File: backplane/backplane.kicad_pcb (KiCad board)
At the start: 2 copper layers, 142.8 x 197.5 mm, 20 parts, among them J1 Conn_01x10, J10 Conn_01x10, J11 Conn_01x10, J2 Conn_01x10, J4 48V in, J5 Conn_01x10, J6 Conn_01x10, J7 Conn_01x10, J8 Conn_01x10, J9 Conn_01x10

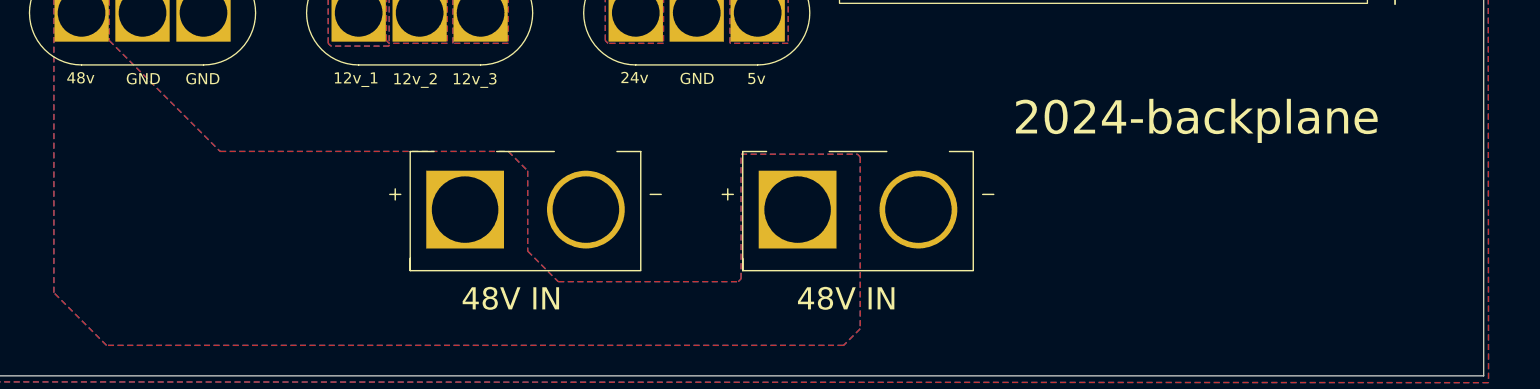
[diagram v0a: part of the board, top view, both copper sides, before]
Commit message: changed font thickness and added contributor
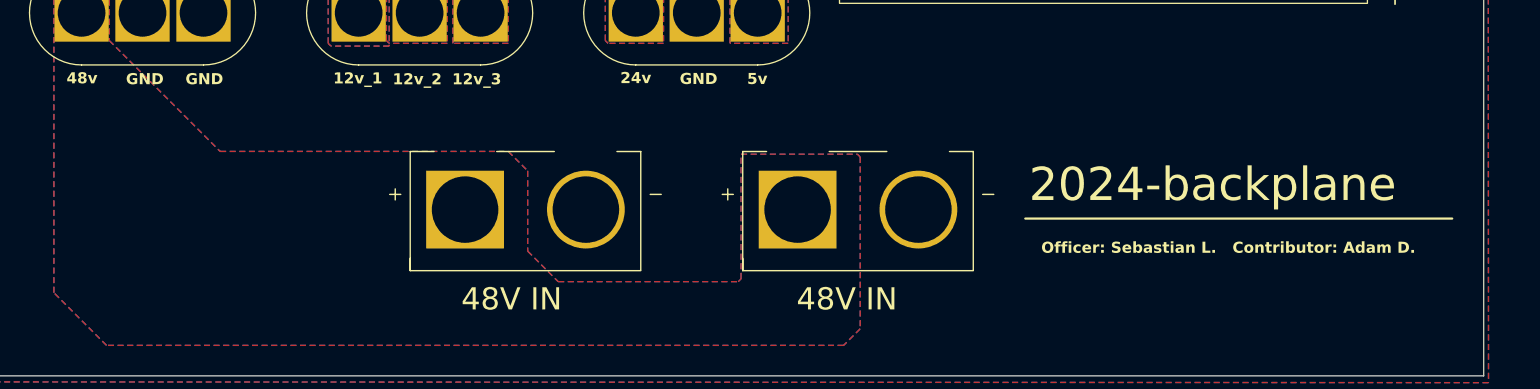
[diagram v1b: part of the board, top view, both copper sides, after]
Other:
- board text added: "Officer: Sebastian L. Contributor: Adam D."
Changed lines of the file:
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@@
   (gr_line (start 241 162.82) (end 241 219.22)
     (stroke (width 0.15) (type default)) (layer "F.SilkS"))
+  (gr_line (start 207.64 238.56) (end 246.16 238.56)
+    (stroke (width 0.2) (type default)) (layer "F.SilkS"))
   (gr_line (start 115 224.76) (end 115 167.24)
     (stroke (width 0.15) (type default)) (layer "F.SilkS"))
@@
   )
   (gr_text "GND" (at 176.46 226.54) (layer "F.SilkS")
-    (effects (font (size 1 1) (thickness 0.15)) (justify left bottom))
+    (effects (font (size 1 1) (thickness 0.2) bold) (justify left bottom))
   )
   (gr_text "12v_2" (at 150.56 226.57) (layer "F.SilkS")
-    (effects (font (size 1 1) (thickness 0.15)) (justify left bottom))
+    (effects (font (size 1 1) (thickness 0.2) bold) (justify left bottom))
   )
   (gr_text "GND" (at 126.5 226.56) (layer "F.SilkS")
-    (effects (font (size 1 1) (thickness 0.15)) (justify left bottom))
+    (effects (font (size 1 1) (thickness 0.2) bold) (justify left bottom))
   )
   (gr_text "12v_1" (at 145.2 226.49) (layer "F.SilkS")
-    (effects (font (size 1 1) (thickness 0.15)) (justify left bottom))
+    (effects (font (size 1 1) (thickness 0.2) bold) (justify left bottom))
   )
   (gr_text "48v" (at 121.14 226.48) (layer "F.SilkS")
-    (effects (font (size 1 1) (thickness 0.15)) (justify left bottom))
+    (effects (font (size 1 1) (thickness 0.2) bold) (justify left bottom))
   )
   (gr_text "POWER" (at 247.25 200.75 90) (layer "F.SilkS")
@@
   )
   (gr_text "GND" (at 131.87 226.56) (layer "F.SilkS")
-    (effects (font (size 1 1) (thickness 0.15)) (justify left bottom))
+    (effects (font (size 1 1) (thickness 0.2) bold) (justify left bottom))
   )
   (gr_text "48V IN" (at 156.75 247) (layer "F.SilkS")
-    (effects (font (size 2 2) (thickness 0.15)) (justify left bottom))
+    (effects (font (size 2 2) (thickness 0.2)) (justify left bottom))
   )
   (gr_text "POWER" (at 113.25 200.75 90) (layer "F.SilkS")
@@
   )
   (gr_text "48V IN" (at 187 247) (layer "F.SilkS")
-    (effects (font (size 2 2) (thickness 0.15)) (justify left bottom))
-  )
-  (gr_text "2024-backplane" (at 206.5 231.25) (layer "F.SilkS")
-    (effects (font (size 3 3) (thickness 0.15)) (justify left bottom))
+    (effects (font (size 2 2) (thickness 0.2)) (justify left bottom))
+  )
+  (gr_text "2024-backplane" (at 207.97 237.25) (layer "F.SilkS")
+    (effects (font (size 3 3) (thickness 0.3)) (justify left bottom))
   )
   (gr_text "12v_3" (at 155.93 226.57) (layer "F.SilkS")
-    (effects (font (size 1 1) (thickness 0.15)) (justify left bottom))
+    (effects (font (size 1 1) (thickness 0.2) bold) (justify left bottom))
   )
   (gr_text "AUX" (at 247.25 156.25 90) (layer "F.SilkS")
@@
   )
   (gr_text "5v" (at 182.54 226.54) (layer "F.SilkS")
-    (effects (font (size 1 1) (thickness 0.15)) (justify left bottom))
+    (effects (font (size 1 1) (thickness 0.2) bold) (justify left bottom))
   )
   (gr_text "ESC" (at 113.25 131.75 90) (layer "F.SilkS")
@@
   )
   (gr_text "24v" (at 171.1 226.46) (layer "F.SilkS")
-    (effects (font (size 1 1) (thickness 0.15)) (justify left bottom))
+    (effects (font (size 1 1) (thickness 0.2) bold) (justify left bottom))
+  )
+  (gr_text "Officer: Sebastian L.   Contributor: Adam D." (at 209.08 241.77) (layer "F.SilkS")
+    (effects (font (size 1 1) (thickness 0.2) bold) (justify left bottom))
   )
   (segment (start 203.265 181.17) (end 203.265 168.73) (width 0.25) (layer "F.Cu") (net 1))
@@
         (xy 106 253.29)
         (xy 106 55)
-        (xy 106 55)
         (xy 249.311431 55)
-        (xy 249.311431 55)
-        (xy 249.435445 253.363647)
       )
     )
